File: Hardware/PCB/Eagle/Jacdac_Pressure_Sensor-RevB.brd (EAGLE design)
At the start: 25 x 25 mm, 31 parts, among them J2 SWD-ADAPTER-, J3 5V, J4 DATA, J5 GND, J6 GND, U1 STM32G030F6P6, U2 XC6206, U3 LPS33HWTR, U4 BAT54S,235

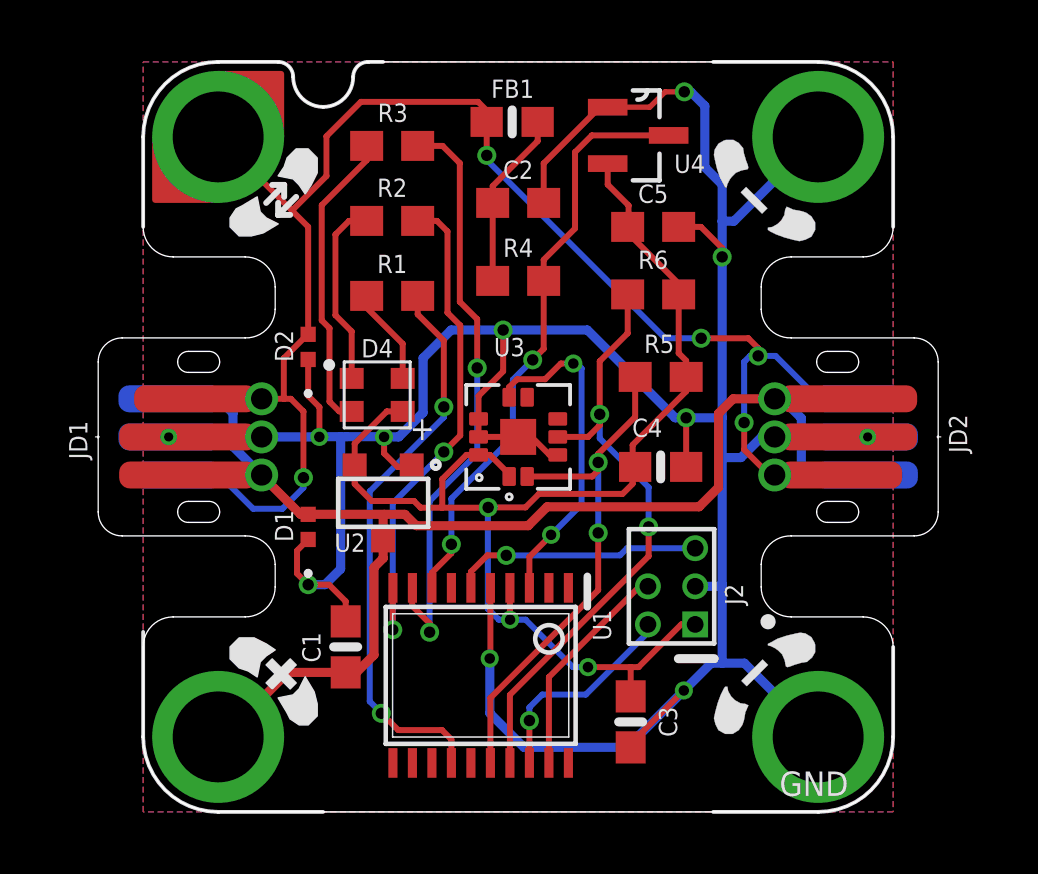
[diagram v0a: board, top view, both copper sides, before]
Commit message: Updated RevB design to match pinouts of other Jacdac modules
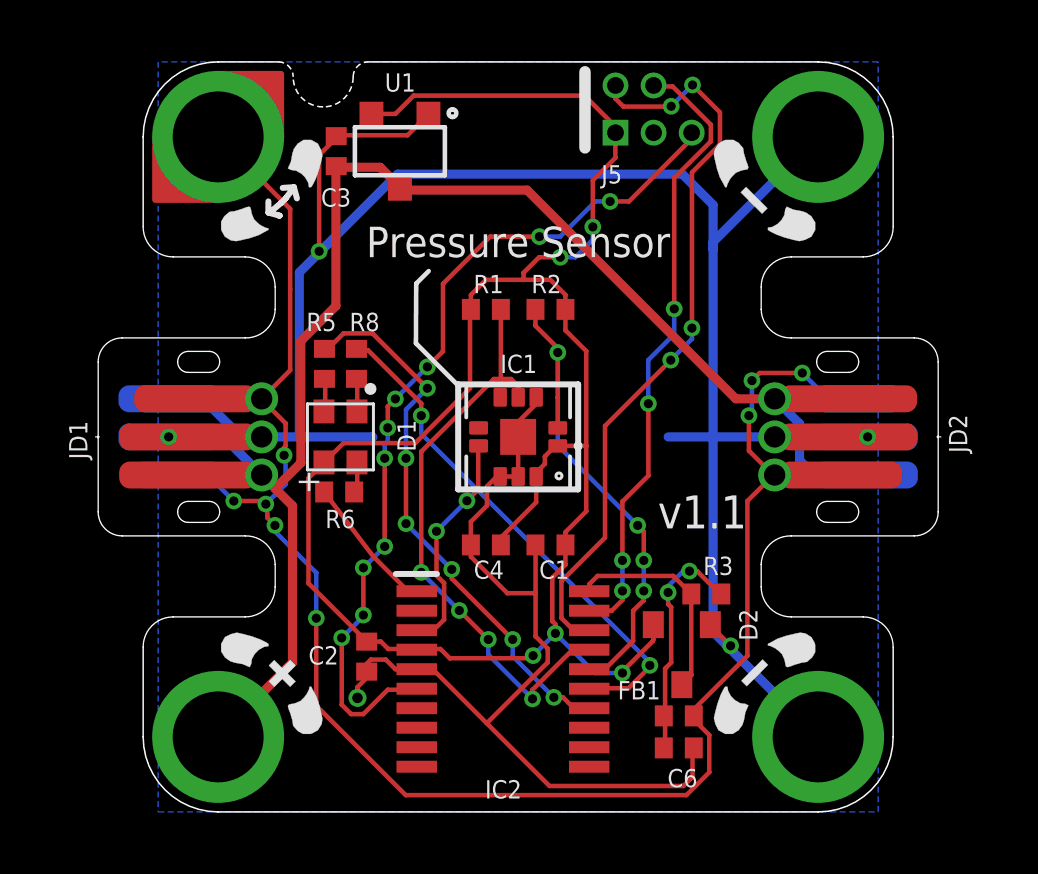
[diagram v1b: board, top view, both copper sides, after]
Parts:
- removed C5: 4.7uF, milador_SMD:0603
- removed D4: C108793, milador_SMD:LED-RGB-2121
- removed J6: GND, milador:M3-HOLE-GND
- removed LABEL_JACDAC_PS: MILADOR-JACDAC-DEVICE-PS, milador:JACDAC-PRESSURE-SENSOR
- removed LABEL_LPS33HW: MILADOR-JACDAC-DEVICE-LPS33HW, milador:JACDAC-LPS33HW
- removed LABEL_MILADOR: MILADOR-LOGO-, milador:MILADOR_LOGO1
- removed LABEL_QR_CODE: MILADOR-QR-CODE-JACDAC-GITHUB-PS, milador:MILADOR_QR_JACDAC_PS
- removed MMC_LOGO: MMC_LOGO-XSM, MMC Eagle:MMC_X-SMALL_LOGO
- removed R4: 220, milador_SMD:0603
- removed U2: XC6206, milador_SMD:SOT23-3-W
- removed U4: BAT54S,235, milador_SMD:SOT23-3
- added C6: 33pF, milador_SMD:0402
- added IC2: STM32G030F6P6, milador_SMD:SOP65P640X120-20N
- added J1: JD, milador:M3-HOLE-DATA
- added LABEL_DEVICE: MILADOR-JACDAC-DEVICE-PS, milador:JACDAC-PRESSURE-SENSOR
- added LABEL_LOGO1: MILADOR-LOGO-SM, milador:MILADOR_LOGO2
- added LABEL_LOGO2: MMC_LOGO-XSM, MMC Eagle:MMC_X-SMALL_LOGO
- added LABEL_LPS33: MILADOR-JACDAC-DEVICE-LPS33HW, milador:JACDAC-LPS33HW
- added LABEL_QRCODE: MILADOR-QR-CODE-JACDAC-GITHUB-PS, milador:MILADOR_QR_JACDAC_PS
- added R8: 150R, milador_SMD:0402
- C1: value 4.7uF -> 0.1uF; device milador_SMD:0603-NO -> milador_SMD:0402
- C2: value 33pF -> 4.7uF; device milador_SMD:0603 -> milador_SMD:0402
- C3, C4: device milador_SMD:0603-NO -> milador_SMD:0402
- D1: value DIODE-ZENER-AA-RCLAMP0521PATCT -> C108793; device milador_SMD:DIODE-ZENER-0402 -> milador_SMD:LED-RGB-2121
- D2: value DIODE-ZENER-AA-RCLAMP0521PATCT -> BAT54S-23-3; device milador_SMD:DIODE-ZENER-0402 -> milador_SMD:SOT23-3
- FB1: value 800mA 1kR -> 1k@100MHz; device milador_SMD:0603-NO -> milador_SMD:0402
- J2: value SWD-ADAPTER- -> PWR; device milador:SWD-ADAPTER -> milador:M3-HOLE-PWR
- J3: value 5V -> GND; device milador:M3-HOLE-PWR-OUTL -> milador:M3-HOLE-GND
- J4: value DATA -> GND; device milador:M3-HOLE-DATA-NOTCH -> milador:M3-HOLE-GND
- J5: value GND -> HACK-CONNECT-5; device milador:M3-HOLE-GND -> milador:HC5-22-62
- R1: value 470 -> 10k; device milador_SMD:0603 -> milador_SMD:0402
- R2: value 150 -> 10k; device milador_SMD:0603 -> milador_SMD:0402
- R3: value 220 -> 220R; device milador_SMD:0603 -> milador_SMD:0402
- R5: value 4.7K -> 220R; device milador_SMD:0603 -> milador_SMD:0402
- R6: value 4.7K -> 470R; device milador_SMD:0603 -> milador_SMD:0402
- U1: value STM32G030F6P6 -> XC6206; device milador_SMD:TSSOP20 -> milador_SMD:SOT23-3-W
- moved C3 21.4 mm to (7.93, 22.0), turned to 90 degrees
- moved FB1 20.6 mm to (19.4, 3.20), turned to 0 degrees
- moved J3 20.0 mm to (24.0, 2.50)
- moved J4 20.0 mm to (24.0, 22.5), turned to 90 degrees
- moved R3 18.2 mm to (20.3, 7.26)
- moved U1 17.7 mm to (10.1, 22.0), turned to 90 degrees
- moved J2 16.3 mm to (4.00, 2.50), turned to 0 degrees
- moved D2 16.1 mm to (19.5, 5.24)
- moved C2 15.9 mm to (8.95, 5.18), turned to 270 degrees
- moved R6 12.4 mm to (8.03, 10.7)
- moved R5 11.2 mm to (7.54, 14.9), turned to 270 degrees
- moved C1 7.63 mm to (15.1, 8.90), turned to 180 degrees
- moved J5 6.76 mm to (17.2, 22.6), turned to 0 degrees
- moved C4 6.38 mm to (12.9, 8.90), turned to 180 degrees
- moved R2 6.04 mm to (15.1, 16.8)
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- renumbered U3 to IC1
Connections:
- removed net +3V3: C3.1, C4.1, C5.1, D4.PLUS, IC1.1, IC1.10, J2.1, R5.2, R6.2, U1.4, U2.2, U4.2
- removed net JD_DATA: R4.2, U1.8, U4.3
- removed net J_DATA: D2.2, FB1.2, J4.H, JD1.1, JD1.6, JD1.P$3, JD2.1, JD2.6, JD2.P$3
- removed net RGB_B: R1.2, U1.14
- removed net RGB_G: R3.2, U1.9
- removed net RGB_R: R2.2, U1.10
- new net JD: D2.3, IC2.20, R3.1
- new net JDF: FB1.2, J1.H, JD1.1, JD1.6, JD1.P$3, JD2.1, JD2.6, JD2.P$3
- new net LED_B: IC2.1, R6.1
- new net LED_G: IC2.14, R5.1
- new net LED_R: IC2.15, R8.1
- new net MISO: IC2.13
- new net PWM: IC2.11
- new net RST: IC2.7
- new net RX/CS: IC2.10
- new net SCK: IC2.8
- new net TX/MOSI: IC2.9
- new net VCC: C1.1, C2.1, C4.1, D1.PLUS, D2.2, IC1.1, IC1.10, IC2.4, J5.1, R1.2, R2.2, U1.2
- net GND: now also C6.2, IC2.5, J3.H, J4.H, J5.3, U1.1; no longer C5.2, D1.1, J2.3, J5.H, J6.H, U1.5, U2.1, U4.1
- net INT: now also IC2.3; no longer U1.3
- net JD5V: now also C3.1, J2.H, U1.3; no longer C1.1, D1.2, J3.H, U2.3
- net N$1: now also C6.1, FB1.1, R3.2; no longer D4.B-, R1.1
- net N$2: now also D1.B-, R6.2; no longer D4.R-, R2.1
- net N$3: now also D1.R-, R8.2; no longer D4.G-, R3.1
- net N$4: now also D1.G-, R5.2; no longer C2.1, FB1.1, R4.1
- net RESET: now also IC2.6, J5.5; no longer J2.5, U1.6
- net SCL: now also IC2.16, R2.1; no longer R5.1, U1.16
- net SDA: now also IC2.17, R1.1; no longer R6.1, U1.17
- net SWCLK: now also IC2.19, J5.4; no longer J2.4, U1.19
- net SWDIO: now also IC2.18, J5.2; no longer J2.2, U1.18
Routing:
- net VCC: track 0.00 -> 64.4 mm, vias 0 -> 5
- net JDF: track 0.00 -> 58.5 mm, vias 0 -> 8
- net J_DATA: track 50.6 -> 0.00 mm, vias 5 -> 0
- net +3V3: track 43.5 -> 0.00 mm, vias 3 -> 0
- net RESET: track 8.34 -> 28.9 mm, vias 1 -> 10
- net RGB_G: track 19.9 -> 0.00 mm, vias 2 -> 0
- net JD_DATA: track 19.9 -> 0.00 mm, vias 2 -> 0
- net RGB_B: track 18.9 -> 0.00 mm, vias 2 -> 0
- net LED_G: track 0.00 -> 18.4 mm, vias 0 -> 6
- net SWDIO: track 7.11 -> 24.9 mm, vias 1 -> 4
- net LED_R: track 0.00 -> 17.2 mm, vias 0 -> 2
- net RGB_R: track 16.9 -> 0.00 mm, vias 2 -> 0
- net SWCLK: track 7.41 -> 20.8 mm, vias 0 -> 4
- net N$3: track 10.1 -> 1.11 mm
- net JD: track 0.00 -> 7.15 mm
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- removed copper zone on layer 1, net GND
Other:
- board text added: "Pressure Sensor"
- board text added: "v1.1"
- board text removed: "GND"
- board text removed: "V1.1"

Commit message: Updated components value
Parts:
- C1, C4: value 0.1uF -> 100nF
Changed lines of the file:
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@@
 </layers>
 <board>
-<fusionsync huburn="a.cGVyc29uYWw6dWUyYWQxOTI2" projecturn="a.cGVyc29uYWw6dWUyYWQxOTI2IzIwMjEwOTEzNDQzNTc2ODA2" f3durn="urn:adsk.wipprod:dm.lineage:5Ap64JYkSlCvhYO3rId2aQ" pcbguid="" lastpulledtime="" lastsyncedchangeguid="" latestrevisionid="cefd08bb-d36f-47cd-880e-06aa6a7b4f2b" lastsyncedrevisionid="cefd08bb-d36f-47cd-880e-06aa6a7b4f2b" lastboardhashguid="768eaca1-4434-f801-6950-d1cafe95f223" lastpushedtime="2022-07-13T07:01:32Z" linktopcb3d="true"/>
+<fusionsync huburn="a.cGVyc29uYWw6dWUyYWQxOTI2" projecturn="a.cGVyc29uYWw6dWUyYWQxOTI2IzIwMjEwOTEzNDQzNTc2ODA2" f3durn="urn:adsk.wipprod:dm.lineage:5Ap64JYkSlCvhYO3rId2aQ" pcbguid="" lastpulledtime="" lastsyncedchangeguid="" latestrevisionid="b947308b-a184-4601-8475-4bf333abcca3" lastsyncedrevisionid="b947308b-a184-4601-8475-4bf333abcca3" lastboardhashguid="ee84bf69-8a14-6a75-bb42-dbff4f4dba65" lastpushedtime="2022-07-14T07:58:23Z" linktopcb3d="true"/>
 <plain>
 <text x="14" y="19" size="1.016" layer="21" font="vector" ratio="13" align="center">Pressure Sensor</text>
@@
 <attribute name="VALUE" x="14.4412" y="15.345" size="0.8128" layer="27" ratio="10"/>
 </element>
-<element name="C1" library="milador_SMD" library_urn="urn:adsk.eagle:library:27847482" package="0402" package3d_urn="urn:adsk.eagle:package:36491935/2" value="0.1uF" x="15.0762" y="8.9" smashed="yes" rot="R180">
+<element name="C1" library="milador_SMD" library_urn="urn:adsk.eagle:library:27847482" package="0402" package3d_urn="urn:adsk.eagle:package:36491935/2" value="100nF" x="15.0762" y="8.9" smashed="yes" rot="R180">
 <attribute name="NAME" x="14.7" y="7.77" size="0.6096" layer="25" font="vector" ratio="20"/>
 <attribute name="VALUE" x="15.7112" y="10.305" size="0.8128" layer="27" ratio="10" rot="R180"/>
 </element>
-<element name="C4" library="milador_SMD" library_urn="urn:adsk.eagle:library:27847482" package="0402" package3d_urn="urn:adsk.eagle:package:36491935/2" value="0.1uF" x="12.9238" y="8.9" smashed="yes" rot="R180">
+<element name="C4" library="milador_SMD" library_urn="urn:adsk.eagle:library:27847482" package="0402" package3d_urn="urn:adsk.eagle:package:36491935/2" value="100nF" x="12.9238" y="8.9" smashed="yes" rot="R180">
 <attribute name="NAME" x="12.5188" y="7.77" size="0.6096" layer="25" font="vector" ratio="20"/>
 <attribute name="VALUE" x="13.5588" y="10.305" size="0.8128" layer="27" ratio="10" rot="R180"/>

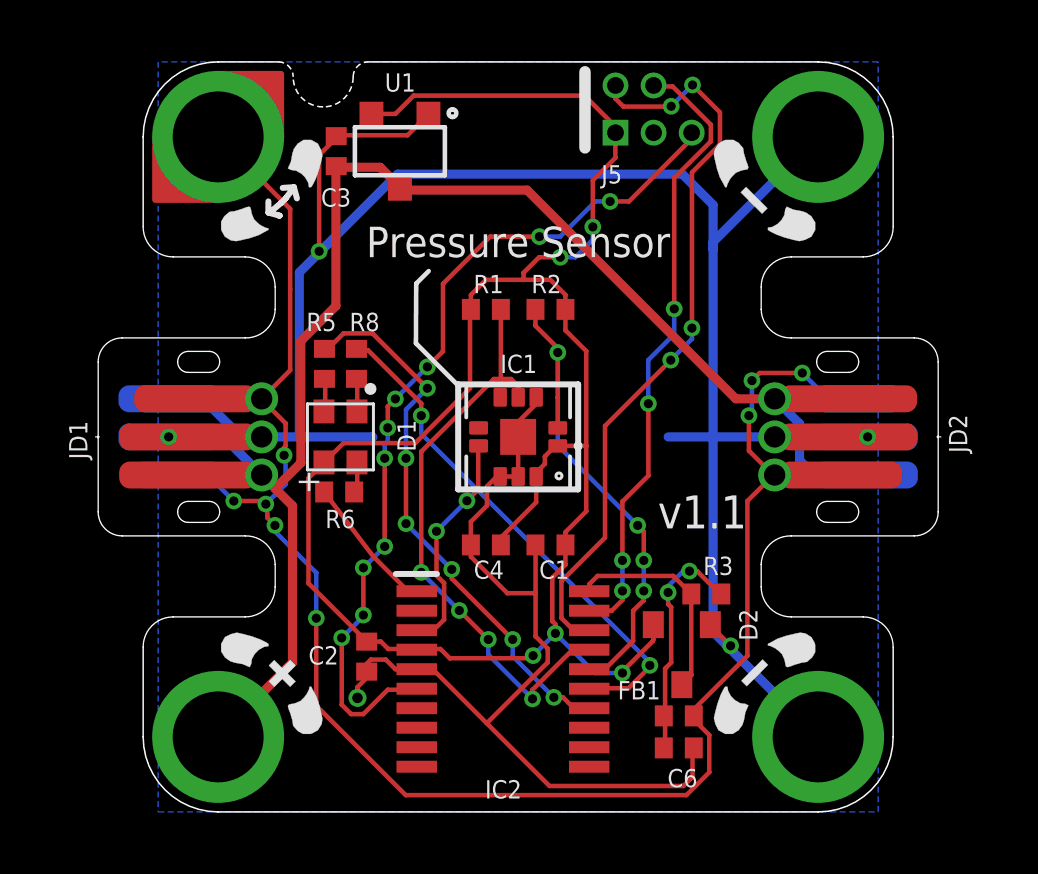
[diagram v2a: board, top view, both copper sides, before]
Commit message: Updated design : Added CS trace
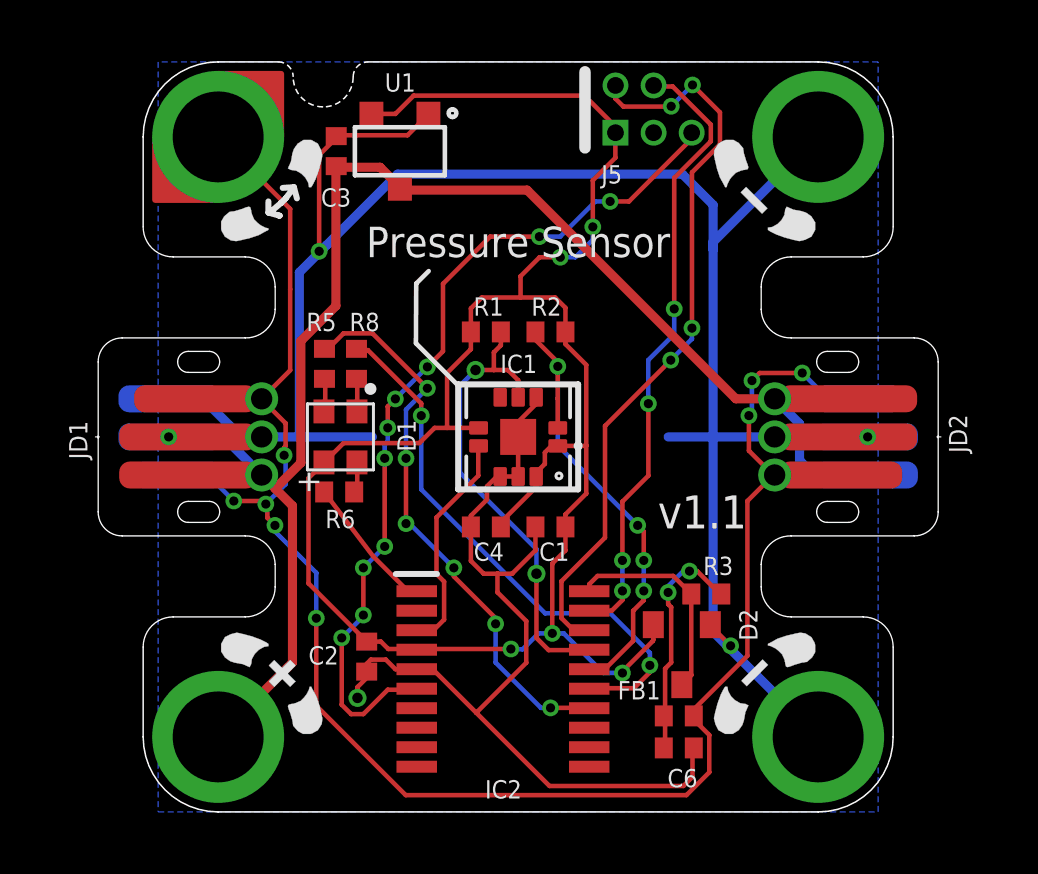
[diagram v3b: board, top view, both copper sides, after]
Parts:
- moved R1 0.75 mm to (12.9, 16.0)
- moved R2 0.75 mm to (15.1, 16.0)
- moved C1 0.60 mm to (15.1, 9.50)
- moved C4 0.60 mm to (12.9, 9.50)
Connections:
- net VCC: now also IC1.6
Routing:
- net SDA: track 19.6 -> 15.6 mm, vias 4 -> 2
- net LED_R: track 17.2 -> 18.6 mm
- net SCL: track 17.1 -> 15.8 mm
- net LED_G: track 18.4 -> 18.9 mm
- net INT: vias 2 -> 0

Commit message: Updated RevB : Added Pull-Up to SA0
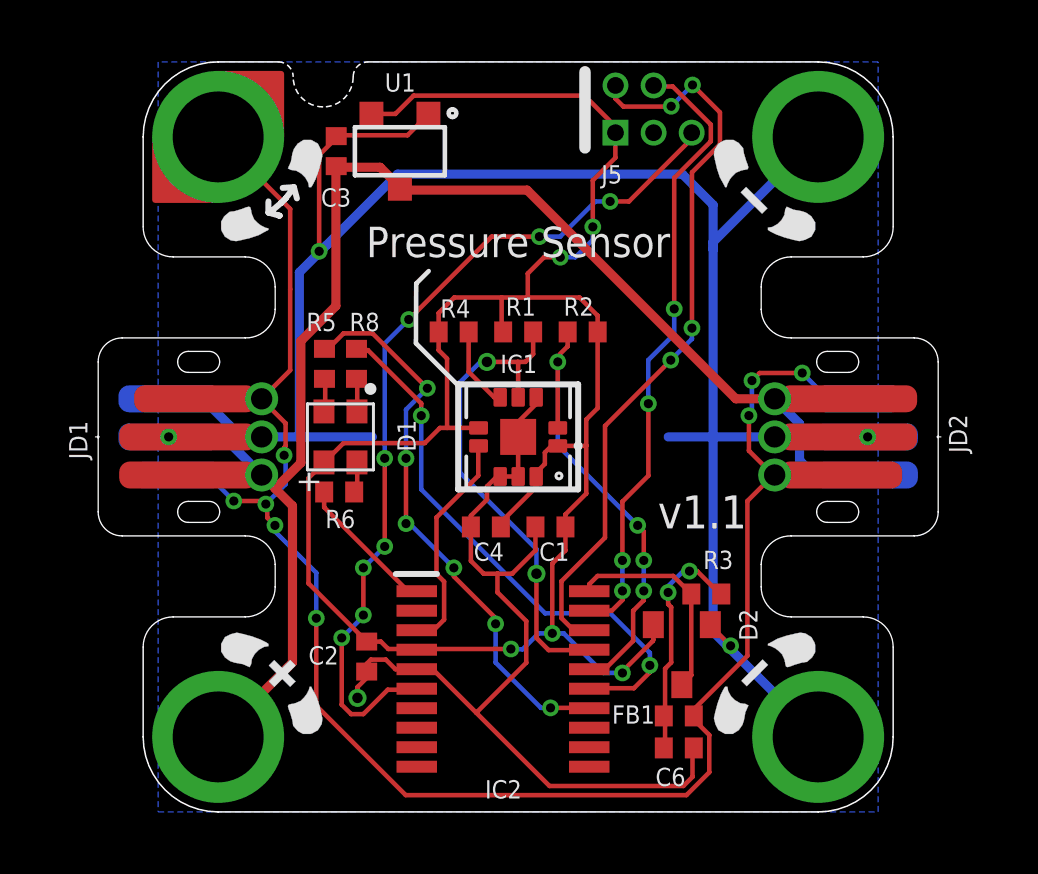
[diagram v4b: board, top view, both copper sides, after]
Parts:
- added R4: 10k, milador_SMD:0402
- moved R1 1.08 mm to (14.0, 16.0)
- moved R2 1.07 mm to (16.1, 16.0)
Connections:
- new net SA0: IC1.5, R4.1
- net VCC: now also R4.2
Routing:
- net SA0: track 0.00 -> 2.73 mm
- net VCC: track 64.6 -> 67.1 mm
- net SDA: track 15.6 -> 16.3 mm
- net RESET: vias 10 -> 8
